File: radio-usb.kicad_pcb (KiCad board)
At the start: 2 copper layers, 127 x 90 mm, 228 parts, among them J1 Barrel_Jack, J10 Conn_Coaxial, J11 ACJS-MHDRM, J12 ACJS-MHDRM, J2 miniUSB, J3 15EDGRC-3.5-03P-14, J4 DB9_Female, J5 EEP_EN, J6 Mini-DIN-6, J7 EDAC 690-008-221-904, J8 DB9_Male, J9 Conn_Coaxial, Q1 BC846C, Q2 BC846, Q3 BC846, Q4 BC846, Q5 BC856, SW1 SW_Push_DPDT, SW2 SW_SPDT, SW3 SW_SPDT, SW4 SW_DIP_x04, SW5 SW_DIP_x04, SW6 SW_DPDT_x2, SW7 SW_SPDT, U1 L7805, U10 AP2171W, U11 TLP2662, U12 TLP2662, U13 MAX3232, U14 93CxxC, U15 PCM2902, U17 FT2232HL, U18 PC817, U19 CRIYCHLEY9000, U2 24LC04, U20 PC817, U21 PC817, U22 CRIYCHLEY9000, U23 LMV321IDBVR, U3 APX809_810-xxSA, U4 AP22814AW5, U5 AP22814AW5, U6 USB2514B_Bi, U7 LM1117-3.3, U8 TBA 1-0511, U9 4069, X1 MAB5SH, Y1 24MHz, Y2 12MHz, Y3 12M

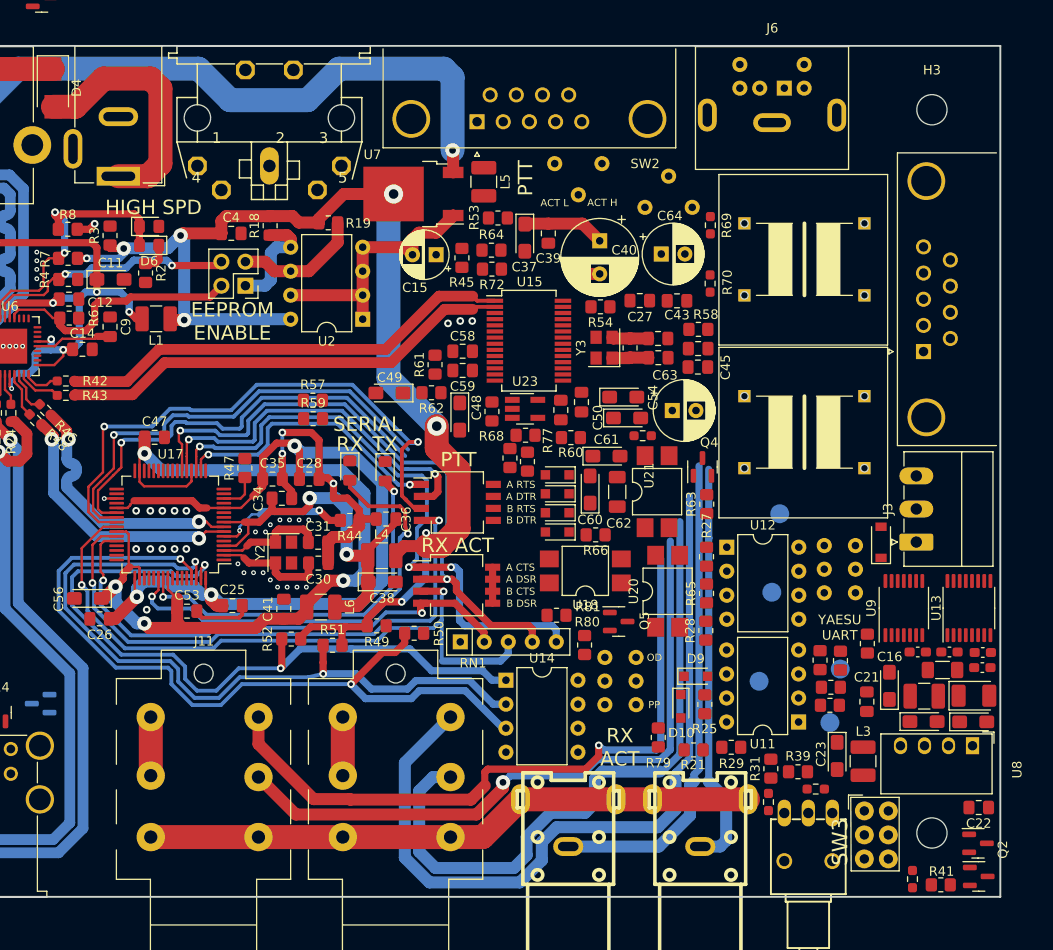
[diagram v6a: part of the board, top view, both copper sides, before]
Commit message: some pcb routing around io
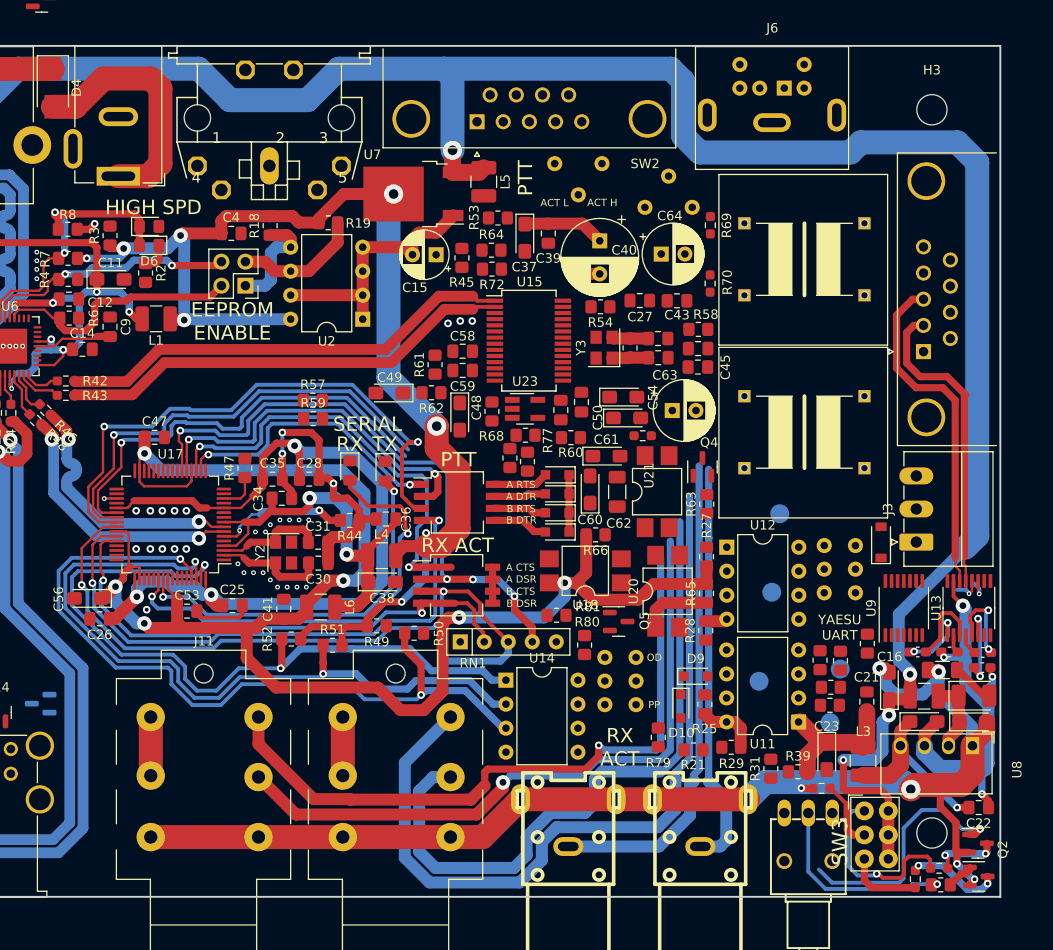
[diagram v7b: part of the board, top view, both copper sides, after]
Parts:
- moved R37 19.4 mm to (158.6, 112.5), turned to 0 degrees
- moved C23 1.09 mm to (146.7, 100.6)
- moved R35 0.61 mm to (146.2, 104.1)
- moved R36 0.30 mm to (156.1, 113.7)
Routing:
- net +5V: track 87.9 -> 244.1 mm, vias 2 -> 5
- net /SER_VCCIO: track 95.2 -> 176.9 mm, vias 4 -> 6
- net GND: track 174.4 -> 242.2 mm, vias 67 -> 73
- net GNDREF: track 0.00 -> 43.8 mm, vias 0 -> 4
- net /RS232TX: track 0.00 -> 36.1 mm
- net /RS232RX: track 0.00 -> 32.8 mm
- net /PTT_CTRL: track 0.00 -> 27.5 mm, vias 0 -> 1
- net Net-(Q2-Pad1): track 0.00 -> 26.2 mm, vias 0 -> 1
- net /DCDC_OUT: track 0.00 -> 19.7 mm, vias 0 -> 1
- net Net-(D12-Pad2): track 0.00 -> 19.5 mm, vias 0 -> 1
- net /SER_A_CTS_IN: track 64.7 -> 46.5 mm, vias 3 -> 2
- net VD: track 0.00 -> 15.5 mm
- net Net-(Q3-Pad3): track 0.00 -> 10.0 mm, vias 0 -> 2
- net /SER_B_CTS_IN: track 70.3 -> 80.0 mm
- net Net-(C29-Pad2): track 0.00 -> 9.17 mm, vias 0 -> 2
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
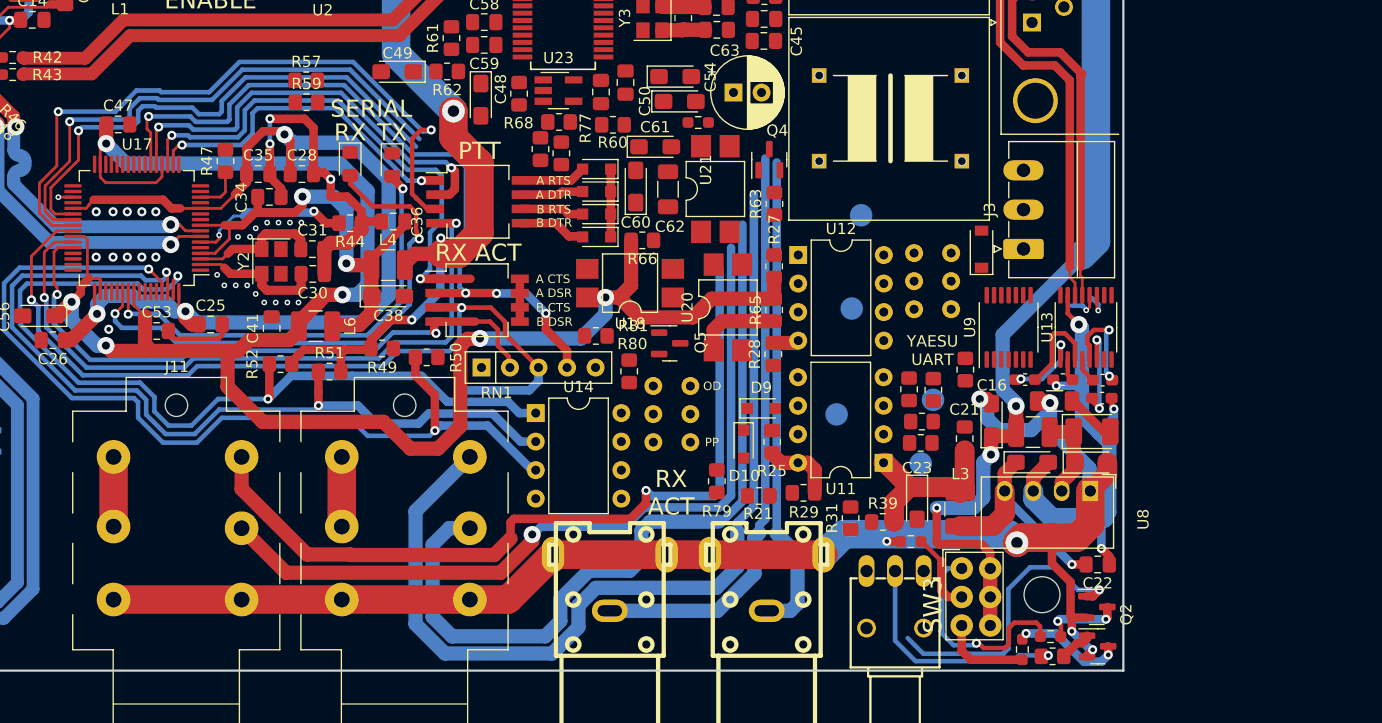
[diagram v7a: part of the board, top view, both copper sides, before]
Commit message: more pcb traces routing
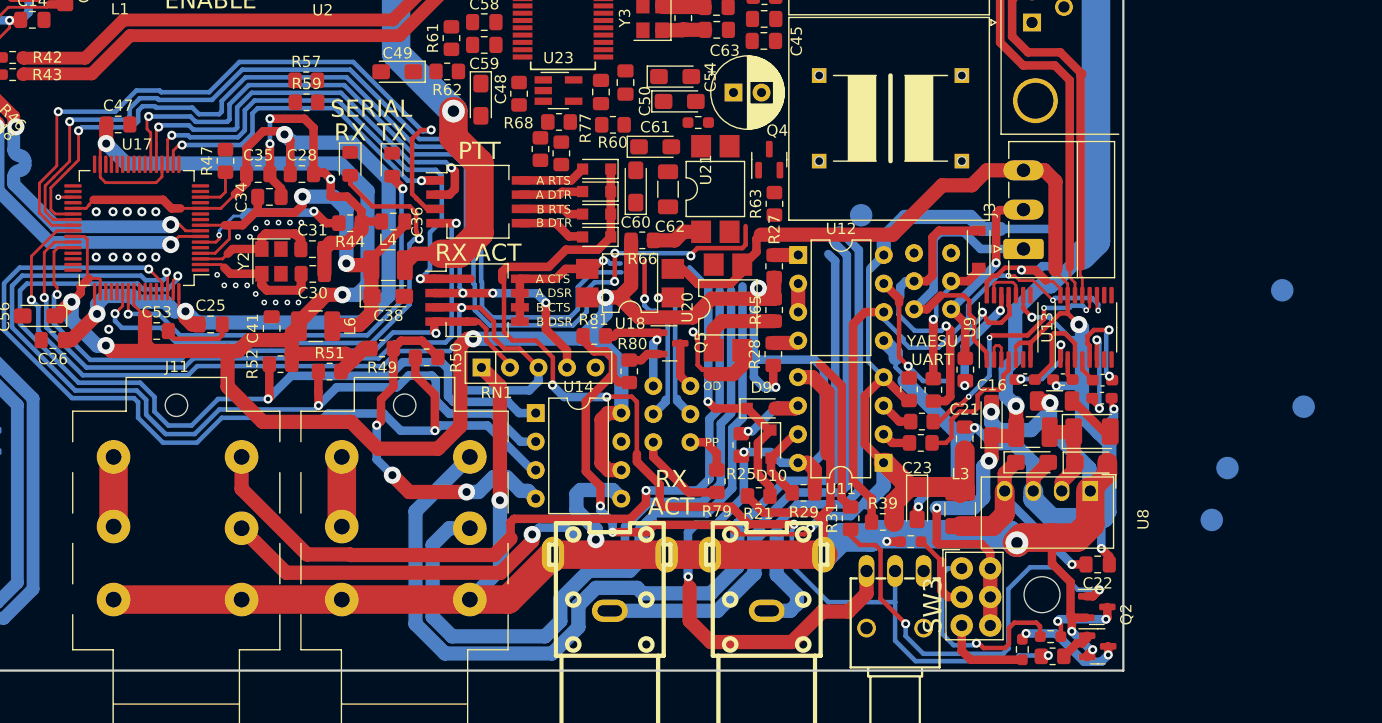
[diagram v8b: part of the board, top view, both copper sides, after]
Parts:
- moved TP9 41.6 mm to (181.2, 92.0)
- moved TP4 38.4 mm to (179.2, 81.7)
- moved TP5 26.9 mm to (174.4, 97.5)
- moved TP7 26.4 mm to (173.0, 102.1)
- moved R25 2.76 mm to (131.1, 95.5)
- moved D10 2.44 mm to (133.7, 95.4)
- moved D7 0.25 mm to (152.2, 78.0)
- moved R81 0.13 mm to (118.0, 85.8), turned to 180 degrees
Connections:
- net AUD_FRM_RADIO renamed AF_FRM_RADIO
- net AUD_TO_RADIO renamed AF_TO_RADIO
- net Net-(J11-PadT) renamed /AF_FRM_RADIO_PREINS
- R49 pad 2: +3V3 -> /SER_VCCIO
- R51 pad 2: +3V3 -> /SER_VCCIO
- R52 pad 2: +3V3 -> /SER_VCCIO
- U14 pad 6: +3V3 -> /SER_VCCIO
- U14 pad 8: +3V3 -> /SER_VCCIO
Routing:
- net VD: track 15.5 -> 126.6 mm, vias 0 -> 4
- net /SER_VCCIO: track 176.9 -> 278.8 mm, vias 6 -> 10
- net GNDREF: track 43.8 -> 144.4 mm, vias 4 -> 7
- net /PTT_CTRL: track 27.5 -> 96.6 mm, vias 1 -> 4
- net /SER_B_RXD_IN: track 47.9 -> 109.0 mm, vias 1 -> 2
- net GND: track 242.2 -> 298.3 mm, vias 73 -> 75
- net /SER_B_TXD_OUT: track 46.4 -> 99.9 mm, vias 1 -> 4
- net /TTL_TX: track 2.76 -> 49.0 mm, vias 1 -> 3
- net Net-(R49-Pad1): track 0.00 -> 32.1 mm, vias 0 -> 3
- net /CAT_UART_RX: track 0.00 -> 27.3 mm
- net PTT: track 0.00 -> 27.0 mm, vias 0 -> 1
- net /TTL_TX_2: track 0.00 -> 25.9 mm, vias 0 -> 2
- net +3V3: track 133.1 -> 108.3 mm, vias 8 -> 6
- net /RX_ACT_SEP: track 3.81 -> 27.4 mm, vias 0 -> 1
- net /TTL_RX: track 2.97 -> 22.2 mm, vias 1 -> 4
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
